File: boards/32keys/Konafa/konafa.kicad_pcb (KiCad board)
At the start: 2 copper layers, 122.6 x 88.9 mm, 24 parts

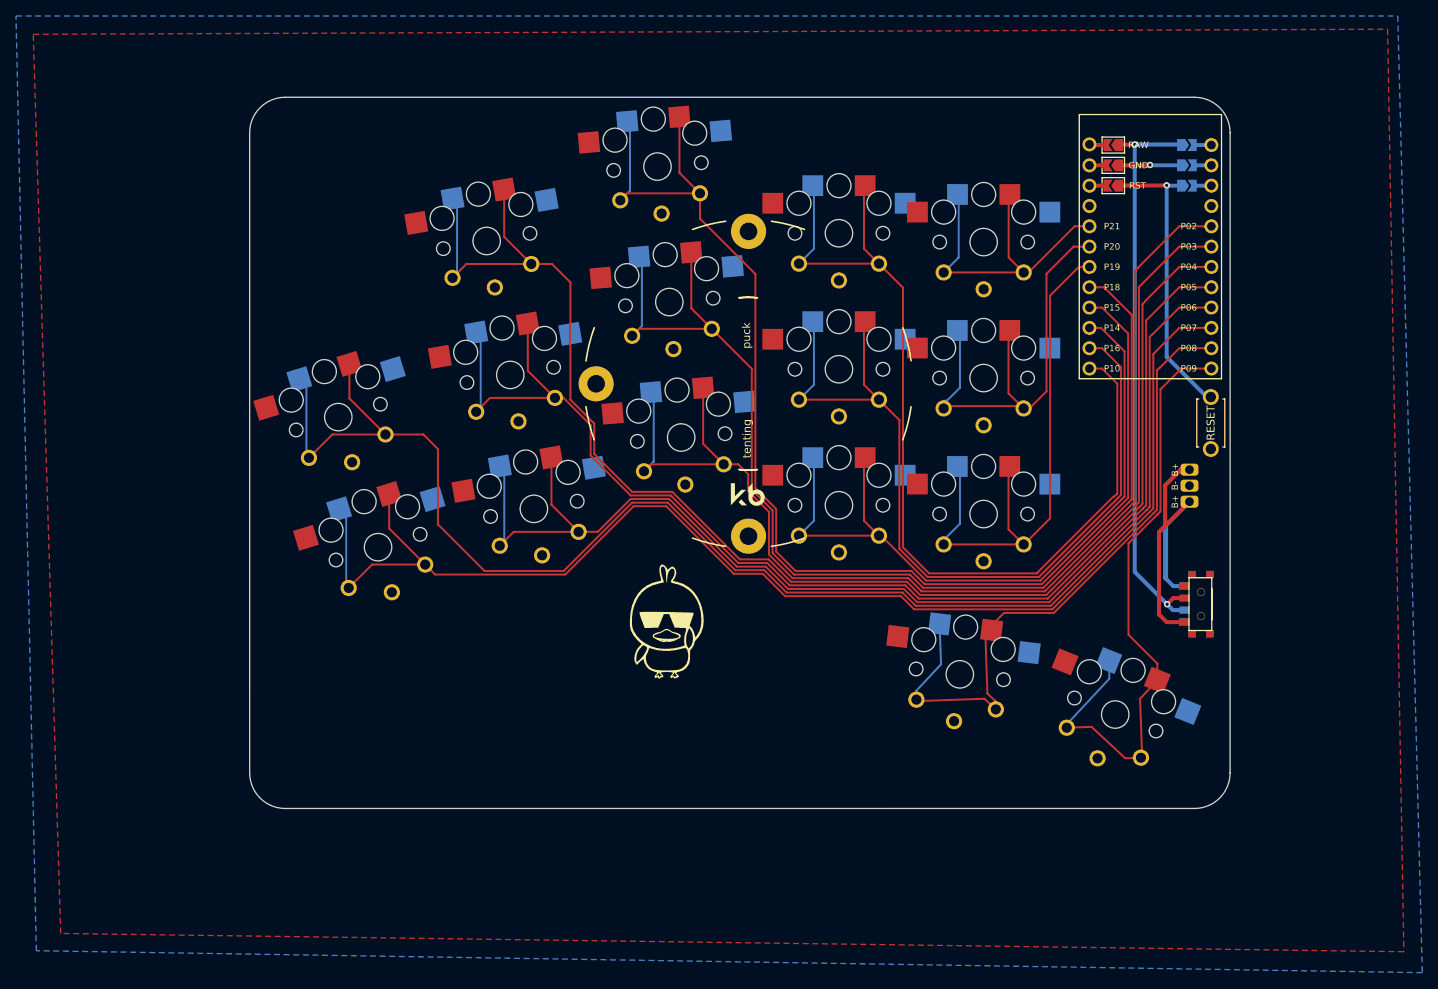
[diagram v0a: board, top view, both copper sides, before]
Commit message: new cases for konafa and battoota
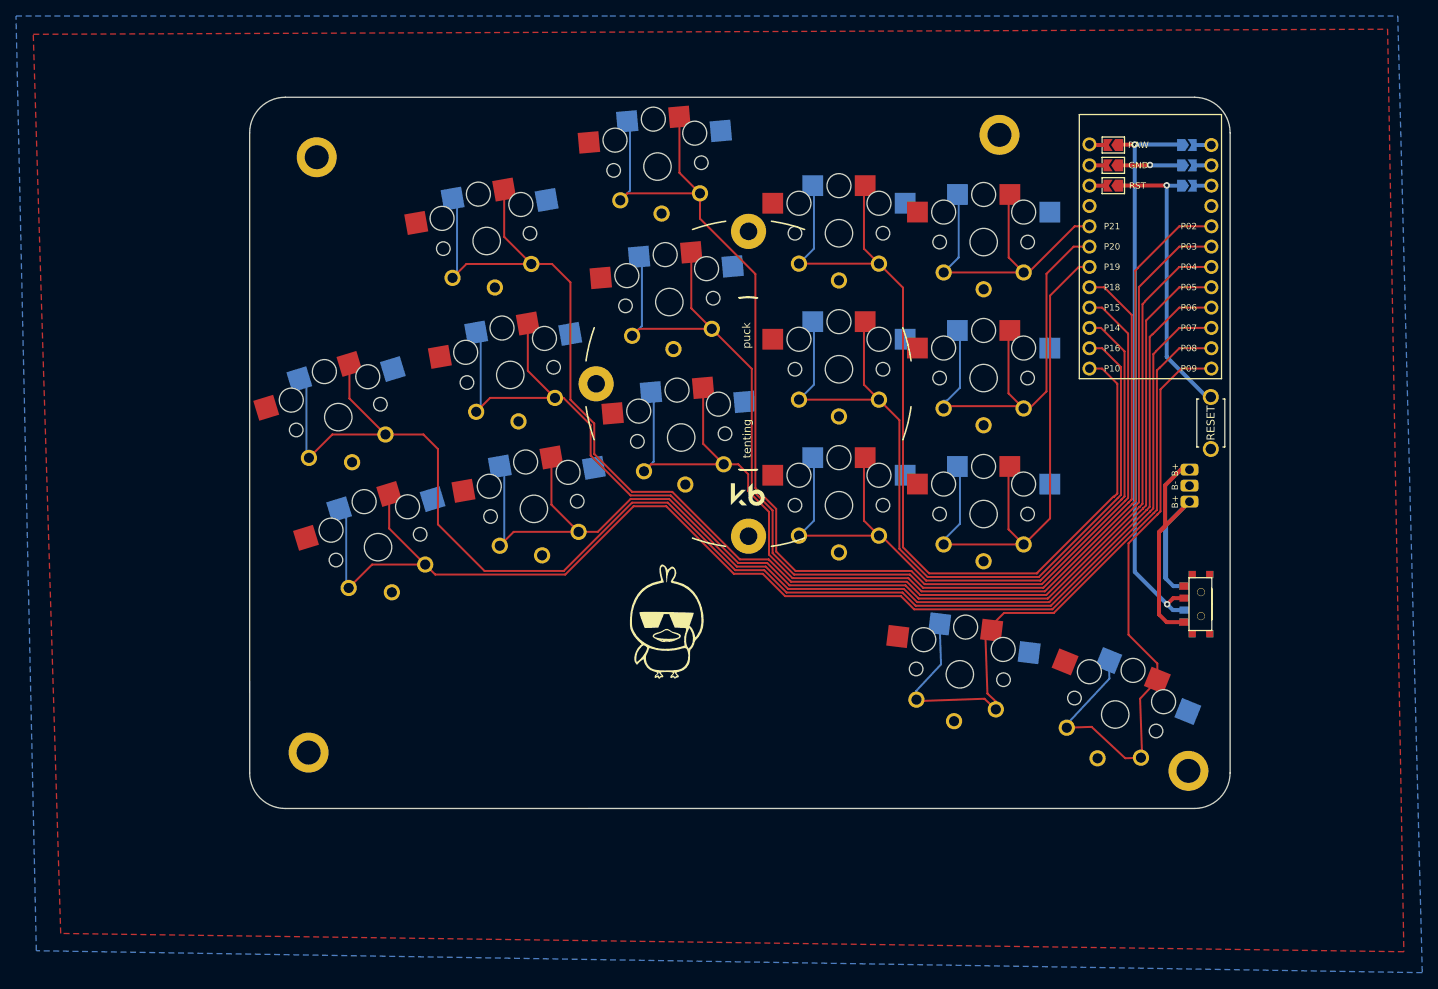
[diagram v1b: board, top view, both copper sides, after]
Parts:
- added ?: , , F.Cu at (49.1, -40.8)
- added ?: , , F.Cu at (50.1, -115.2)
- added ?: , , F.Cu at (159.1, -38.5)
- added ?: , , F.Cu at (135.5, -118.0)
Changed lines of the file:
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@@
       (net 2 "GND"))
+  )
+  (footprint "" (layer "F.Cu")
+    (at 49.130791 -40.793254)
+    (fp_text reference "" (at 0 0) (layer "F.SilkS")
+      (effects (font (size 1.27 1.27) (thickness 0.15)))
+    )
+    (fp_text value "" (at 0 0) (layer "F.SilkS")
+      (effects (font (size 1.27 1.27) (thickness 0.15)))
+    )
+    (pad "1" thru_hole circle (at 0 0) (size 5 5) (drill 3) (layers *.Cu *.Mask)
+      (pinfunction "1") (pintype "input"))
   )
   (footprint "E73:SPDT_C128955" (layer "F.Cu")
@@
     (pad "2" smd rect (at 8.275 -3.749999) (size 2.6 2.6) (layers "B.Cu" "B.Paste" "B.Mask")
       (net 2 "GND"))
+  )
+  (footprint "" (layer "F.Cu")
+    (at 50.146791 -115.215254)
+    (fp_text reference "" (at 0 0) (layer "F.SilkS")
+      (effects (font (size 1.27 1.27) (thickness 0.15)))
+    )
+    (fp_text value "" (at 0 0) (layer "F.SilkS")
+      (effects (font (size 1.27 1.27) (thickness 0.15)))
+    )
+    (pad "1" thru_hole circle (at 0 0) (size 5 5) (drill 3) (layers *.Cu *.Mask)
+      (pinfunction "1") (pintype "input"))
   )
   (footprint "LOGO" (layer "F.Cu")
@@
       (net 2 "GND"))
   )
+  (footprint "" (layer "F.Cu")
+    (at 159.112791 -38.507254)
+    (fp_text reference "" (at 0 0) (layer "F.SilkS")
+      (effects (font (size 1.27 1.27) (thickness 0.15)))
+    )
+    (fp_text value "" (at 0 0) (layer "F.SilkS")
+      (effects (font (size 1.27 1.27) (thickness 0.15)))
+    )
+    (pad "1" thru_hole circle (at 0 0) (size 5 5) (drill 3) (layers *.Cu *.Mask)
+      (pinfunction "1") (pintype "input"))
+  )
+  (footprint "" (layer "F.Cu")
+    (at 135.490791 -118.009254)
+    (fp_text reference "" (at 0 0) (layer "F.SilkS")
+      (effects (font (size 1.27 1.27) (thickness 0.15)))
+    )
+    (fp_text value "" (at 0 0) (layer "F.SilkS")
+      (effects (font (size 1.27 1.27) (thickness 0.15)))
+    )
+    (pad "1" thru_hole circle (at 0 0) (size 5 5) (drill 3) (layers *.Cu *.Mask)
+      (pinfunction "1") (pintype "input"))
+  )
   (footprint "Alaa:choc_hotswap_key" (layer "F.Cu")
